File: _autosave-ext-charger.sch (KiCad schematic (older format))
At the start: 61 parts

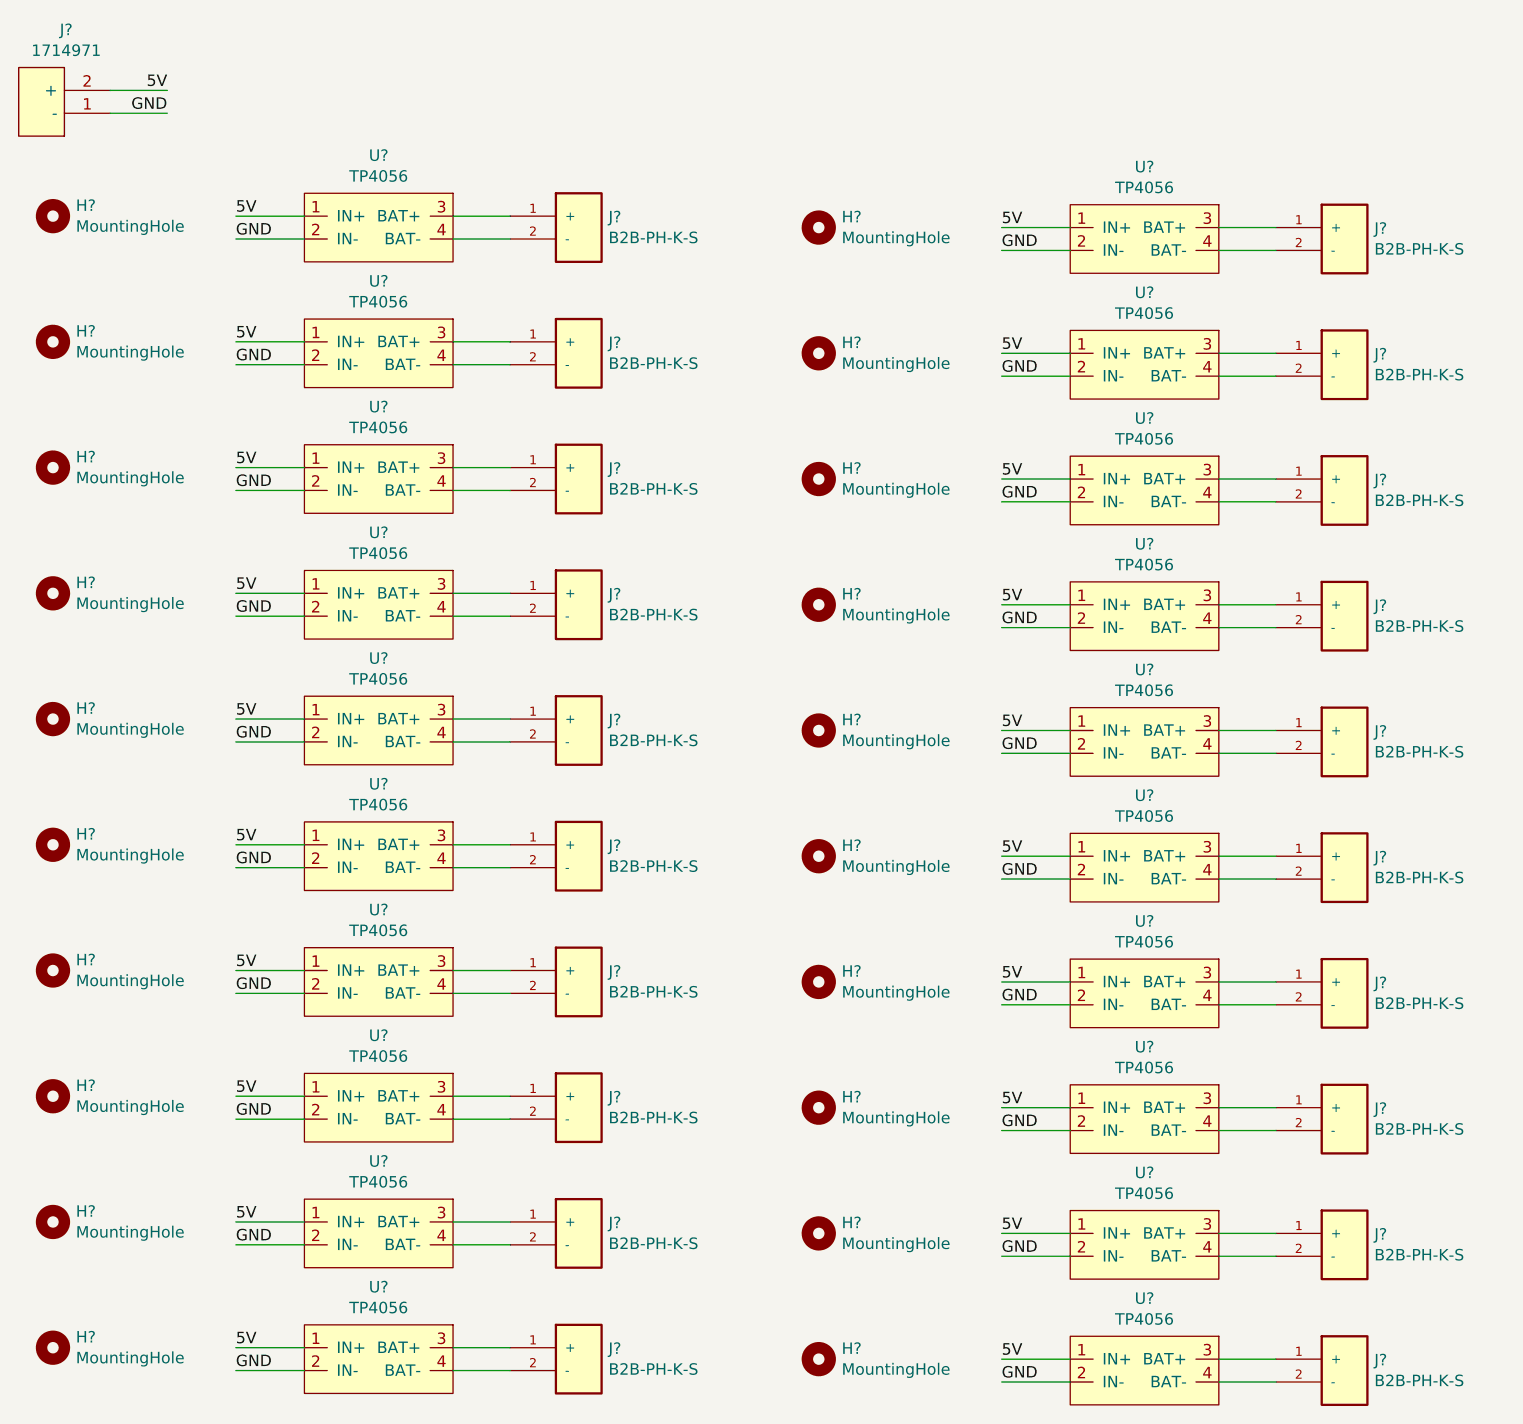
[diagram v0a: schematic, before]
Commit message: created the schematic
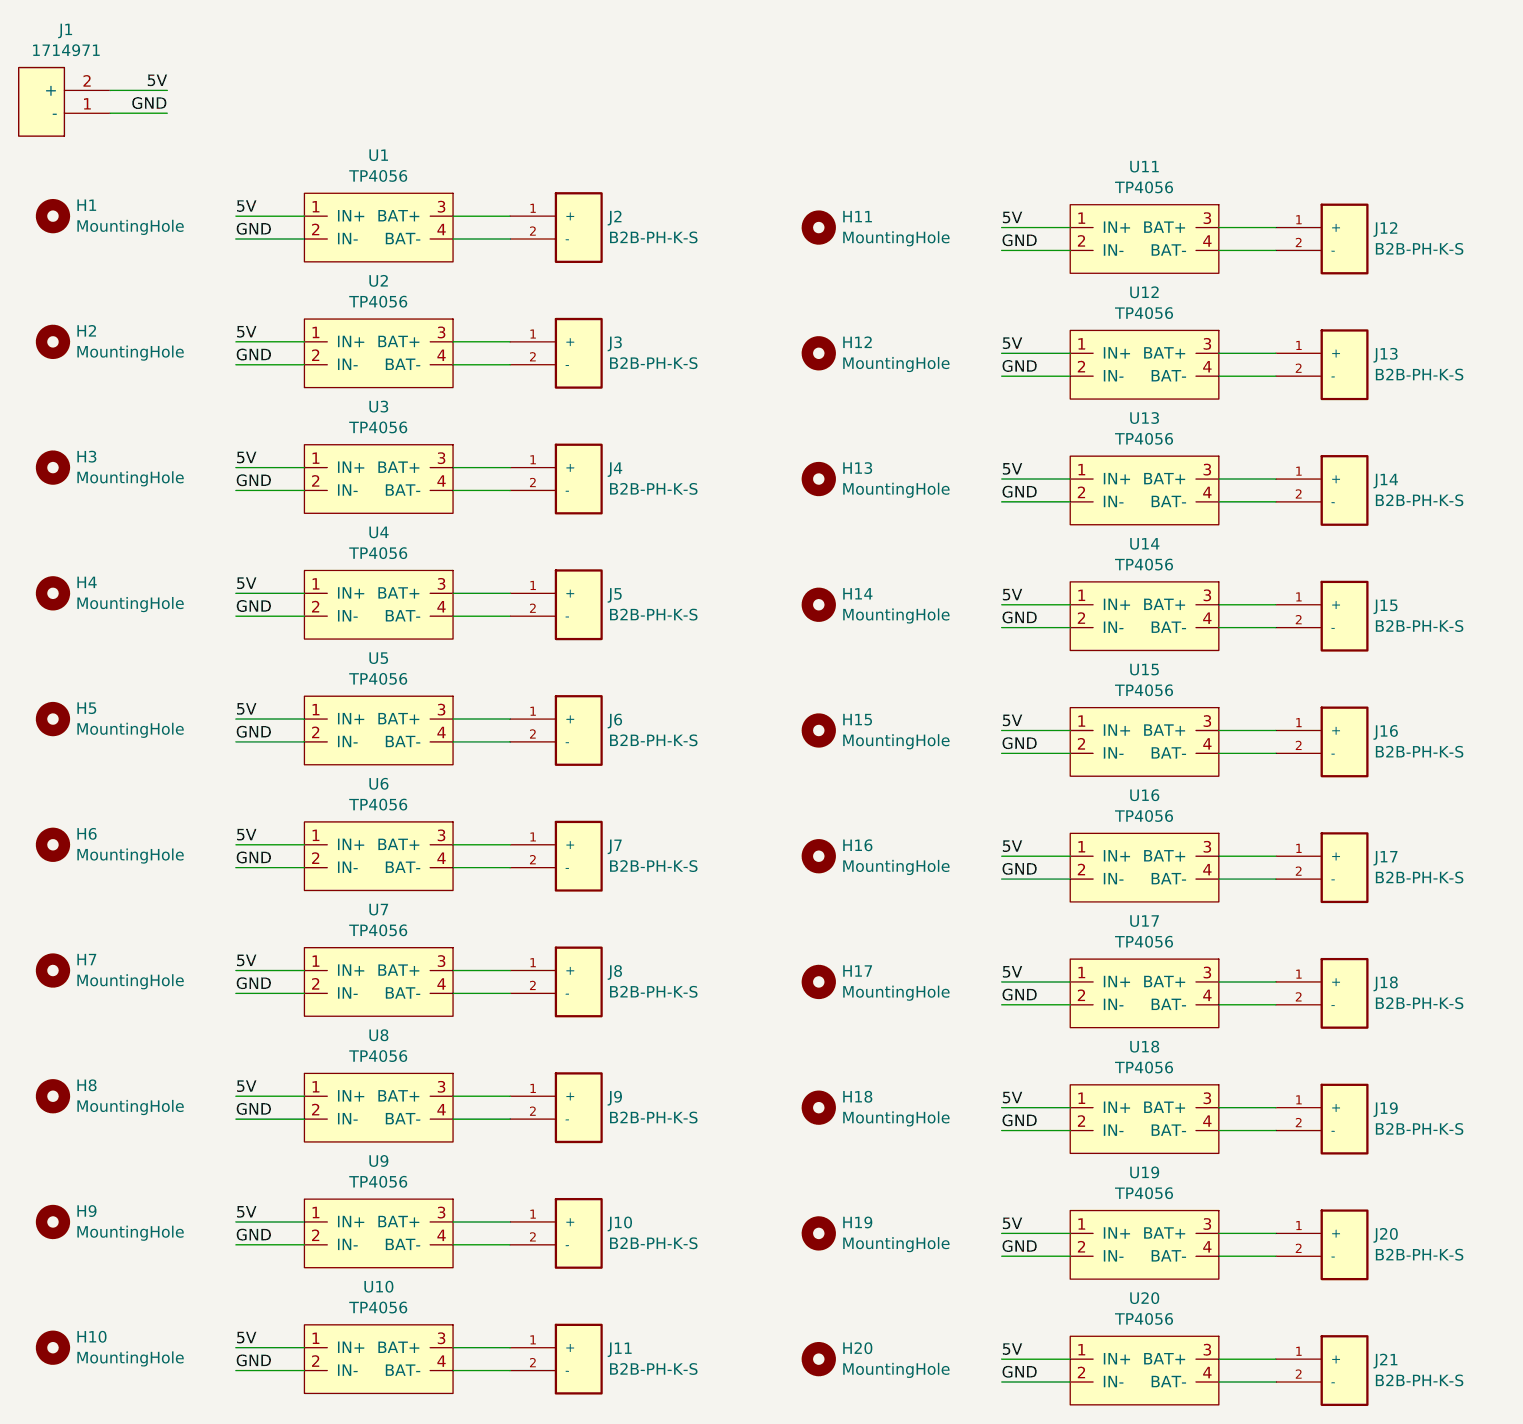
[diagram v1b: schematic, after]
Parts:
- gave numbers to parts that had none: 61
